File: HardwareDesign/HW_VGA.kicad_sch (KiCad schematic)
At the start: 6 parts, among them J1 Conn_02x40_Odd_Even, J401 Conn_01x06, U1 25.175 MHz, U301 GAL22V10

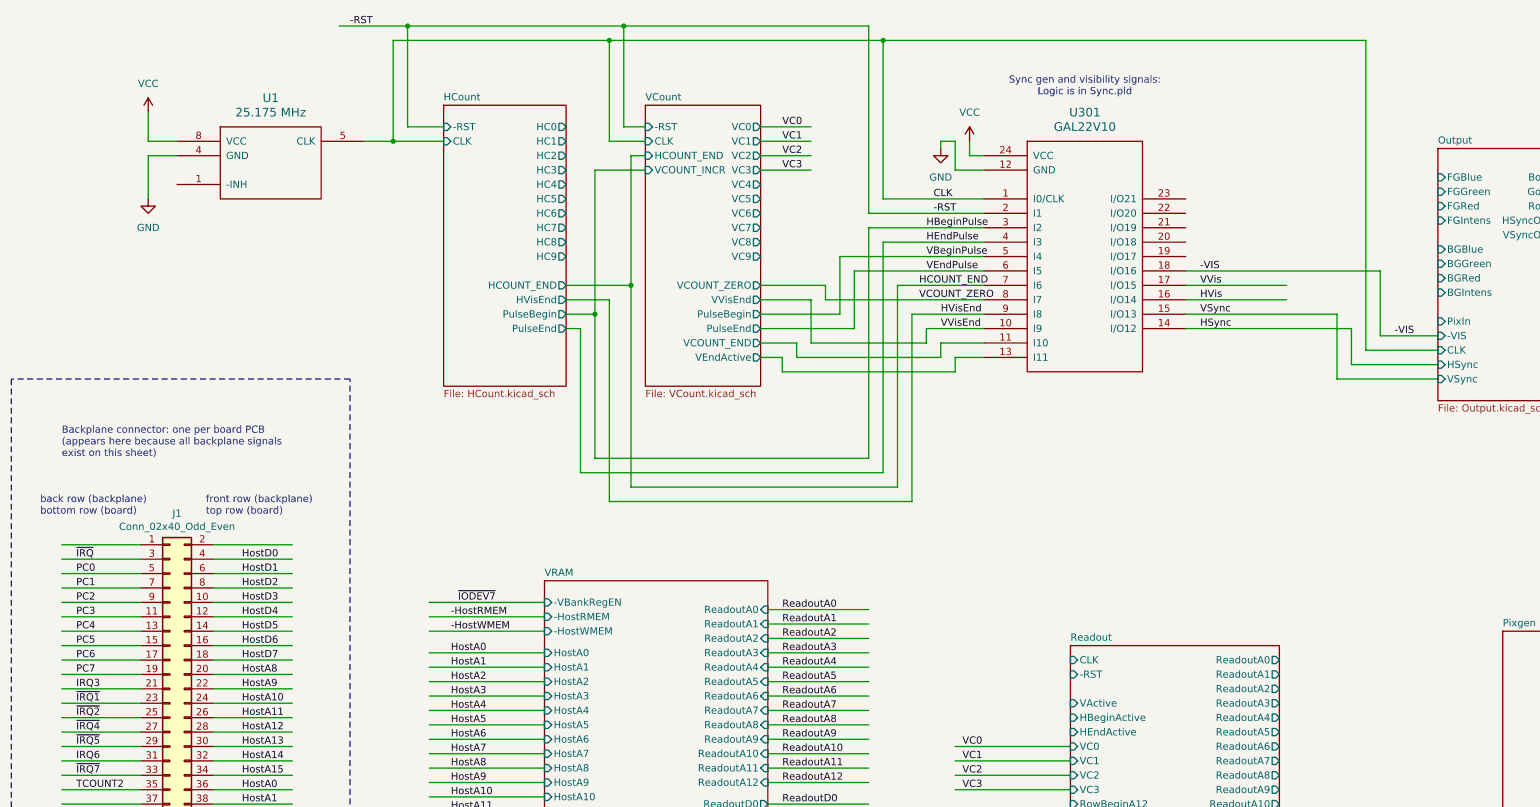
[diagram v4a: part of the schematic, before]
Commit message: use net labels rather than wires on main page
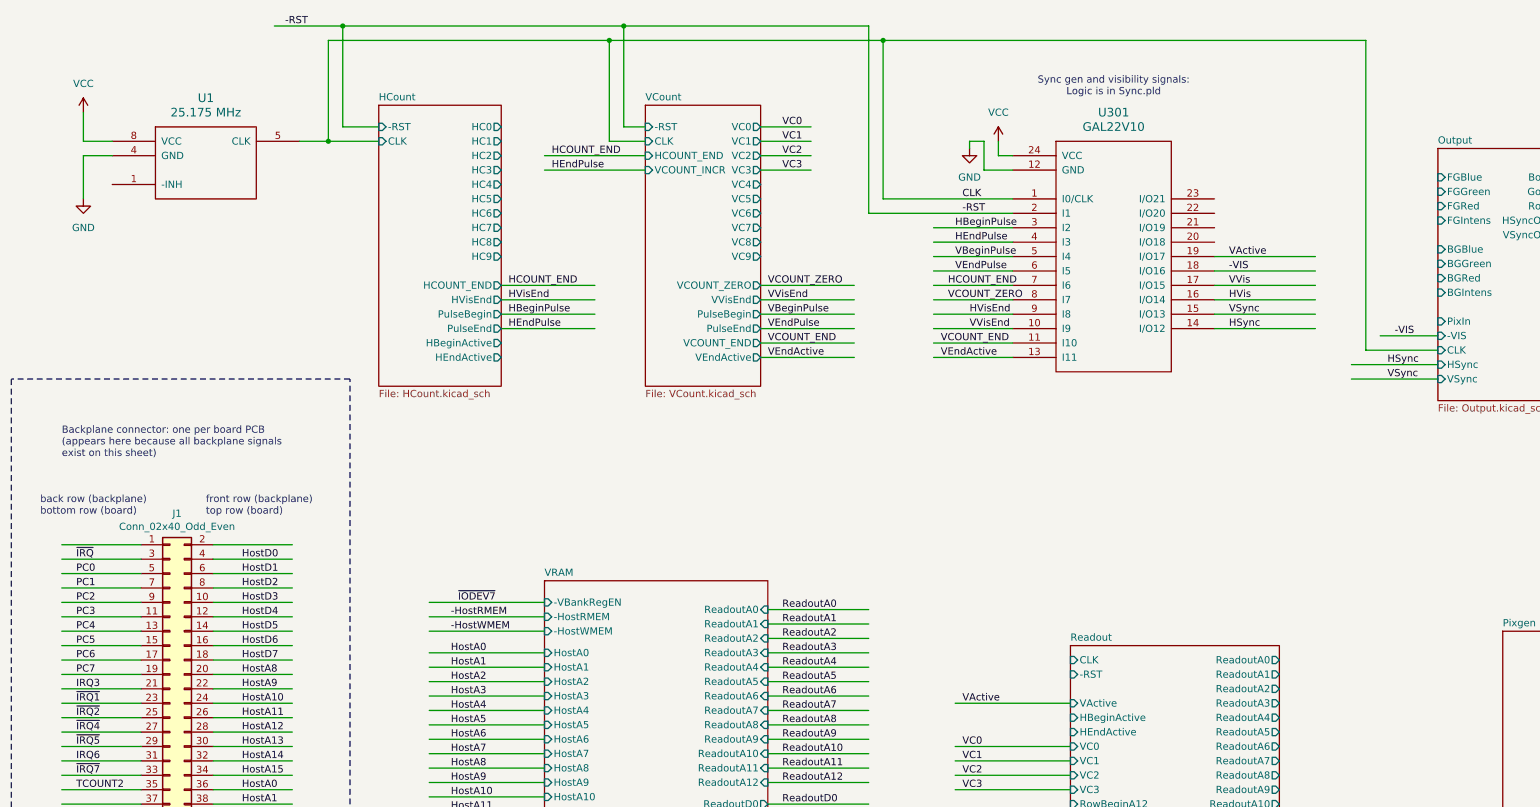
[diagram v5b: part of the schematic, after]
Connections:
- net VActive: now reaches U301.19 (I/O17)
- net VCount/VCOUNT_END renamed VCOUNT_END
- net VCount/VEndActive renamed VEndActive
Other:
- sheet HCount ports: added HBeginActive, HEndActive; removed none
- moved on the sheet: U1, U301
